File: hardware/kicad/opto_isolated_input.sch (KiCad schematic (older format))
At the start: 6 parts, among them Q1 BC547, Q2 BC337, U5 SFH617A-1

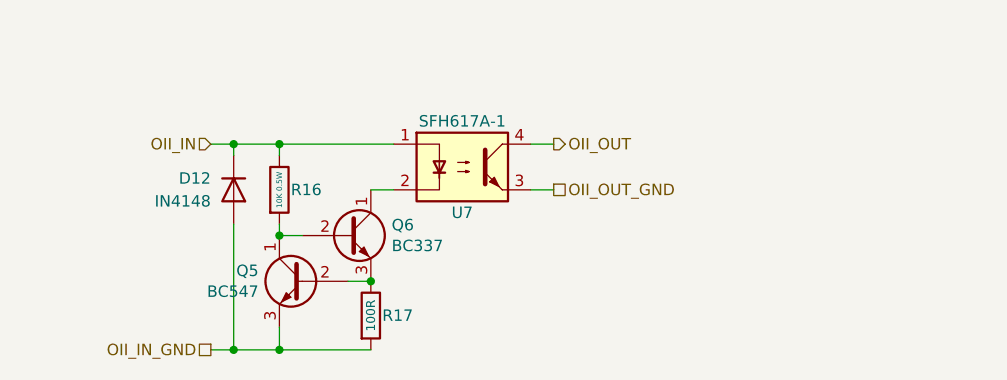
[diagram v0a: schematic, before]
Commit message: New board size
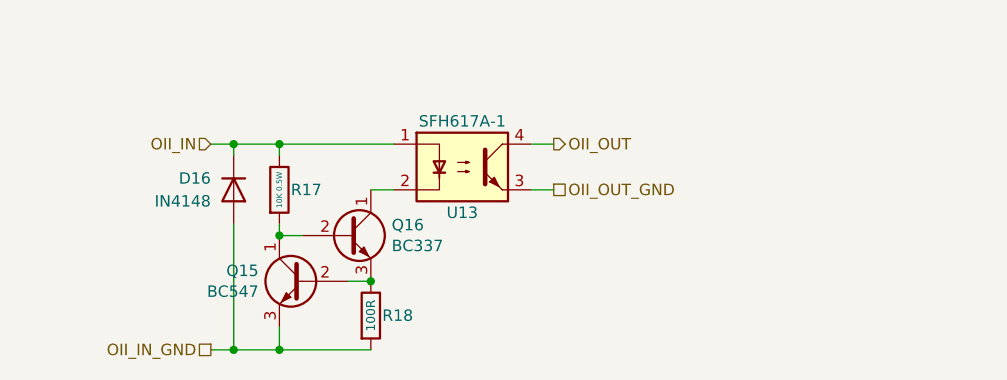
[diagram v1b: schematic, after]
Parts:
- renumbered D10 to D9, R12 to R3, R13 to R4, U5 to U6
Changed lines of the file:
@@
 $EndDescr
 $Comp
-L Isolator:SFH617A-1 U5
+L Isolator:SFH617A-1 U6
 U 1 1 62EBA913
 P 6100 3400
-AR Path="/62FB7846/62EBA913" Ref="U5"  Part="1"
-AR Path="/63089671/62EBA913" Ref="U6"  Part="1"
-AR Path="/63103CAF/62EBA913" Ref="U7"  Part="1"
-AR Path="/62F64647/62EBA913" Ref="U8"  Part="1"
-AR Path="/62FD589D/62EBA913" Ref="U9"  Part="1"
-AR Path="/63041ECA/62EBA913" Ref="U10"  Part="1"
-AR Path="/62F45EE0/62EBA913" Ref="U11"  Part="1"
-AR Path="/62FB890E/62EBA913" Ref="U12"  Part="1"
-F 0 "U7" H 6100 3200 50  0000 C CNN
+AR Path="/62FB7846/62EBA913" Ref="U6"  Part="1"
+AR Path="/63089671/62EBA913" Ref="U7"  Part="1"
+AR Path="/63103CAF/62EBA913" Ref="U8"  Part="1"
+AR Path="/62F64647/62EBA913" Ref="U9"  Part="1"
+AR Path="/62FD589D/62EBA913" Ref="U10"  Part="1"
+AR Path="/63041ECA/62EBA913" Ref="U11"  Part="1"
+AR Path="/62F45EE0/62EBA913" Ref="U12"  Part="1"
+AR Path="/62FB890E/62EBA913" Ref="U13"  Part="1"
+F 0 "U13" H 6100 3200 50  0000 C CNN
 F 1 "SFH617A-1" H 6100 3600 50  0000 C CNN
 F 2 "Package_DIP:DIP-4_W7.62mm" H 5900 3200 50  0001 L CIN
@@
 	5800 3500 5700 3500
 $Comp
-L Device:R R12
+L Device:R R3
 U 1 1 62ED7963
 P 5300 3500
-AR Path="/62FB7846/62ED7963" Ref="R12"  Part="1"
-AR Path="/63089671/62ED7963" Ref="R14"  Part="1"
-AR Path="/63103CAF/62ED7963" Ref="R16"  Part="1"
-AR Path="/62F64647/62ED7963" Ref="R18"  Part="1"
-AR Path="/62FD589D/62ED7963" Ref="R20"  Part="1"
-AR Path="/63041ECA/62ED7963" Ref="R22"  Part="1"
-AR Path="/62F45EE0/62ED7963" Ref="R24"  Part="1"
-AR Path="/62FB890E/62ED7963" Ref="R26"  Part="1"
-F 0 "R16" H 5350 3500 50  0000 L CNN
+AR Path="/62FB7846/62ED7963" Ref="R3"  Part="1"
+AR Path="/63089671/62ED7963" Ref="R5"  Part="1"
+AR Path="/63103CAF/62ED7963" Ref="R7"  Part="1"
+AR Path="/62F64647/62ED7963" Ref="R9"  Part="1"
+AR Path="/62FD589D/62ED7963" Ref="R11"  Part="1"
+AR Path="/63041ECA/62ED7963" Ref="R13"  Part="1"
+AR Path="/62F45EE0/62ED7963" Ref="R15"  Part="1"
+AR Path="/62FB890E/62ED7963" Ref="R17"  Part="1"
+F 0 "R17" H 5350 3500 50  0000 L CNN
 F 1 "10K 0.5W" V 5300 3500 24  0000 C CNN
 F 2 "Resistor_THT:R_Axial_DIN0207_L6.3mm_D2.5mm_P2.54mm_Vertical" V 5230 3500 50  0001 C CNN
@@
 Connection ~ 5300 3300
 $Comp
-L Device:R R13
+L Device:R R4
 U 1 1 62F493CD
 P 5700 4050
-AR Path="/62FB7846/62F493CD" Ref="R13"  Part="1"
-AR Path="/63089671/62F493CD" Ref="R15"  Part="1"
-AR Path="/63103CAF/62F493CD" Ref="R17"  Part="1"
-AR Path="/62F64647/62F493CD" Ref="R19"  Part="1"
-AR Path="/62FD589D/62F493CD" Ref="R21"  Part="1"
-AR Path="/63041ECA/62F493CD" Ref="R23"  Part="1"
-AR Path="/62F45EE0/62F493CD" Ref="R25"  Part="1"
-AR Path="/62FB890E/62F493CD" Ref="R27"  Part="1"
-F 0 "R17" H 5750 4050 50  0000 L CNN
+AR Path="/62FB7846/62F493CD" Ref="R4"  Part="1"
+AR Path="/63089671/62F493CD" Ref="R6"  Part="1"
+AR Path="/63103CAF/62F493CD" Ref="R8"  Part="1"
+AR Path="/62F64647/62F493CD" Ref="R10"  Part="1"
+AR Path="/62FD589D/62F493CD" Ref="R12"  Part="1"
+AR Path="/63041ECA/62F493CD" Ref="R14"  Part="1"
+AR Path="/62F45EE0/62F493CD" Ref="R16"  Part="1"
+AR Path="/62FB890E/62F493CD" Ref="R18"  Part="1"
+F 0 "R18" H 5750 4050 50  0000 L CNN
 F 1 "100R" V 5700 4050 39  0000 C CNN
 F 2 "Resistor_THT:R_Axial_DIN0207_L6.3mm_D2.5mm_P2.54mm_Vertical" V 5630 4050 50  0001 C CNN
@@
 AR Path="/62F45EE0/62EA87F7" Ref="Q14"  Part="1"
 AR Path="/62FB890E/62EA87F7" Ref="Q16"  Part="1"
-F 0 "Q6" H 5791 3746 50  0000 L CNN
+F 0 "Q16" H 5791 3746 50  0000 L CNN
 F 1 "BC337" H 5791 3655 50  0000 L CNN
 F 2 "Package_TO_SOT_THT:TO-92_Inline" H 5800 3625 50  0001 L CIN
@@
 Connection ~ 5300 4200
 $Comp
-L Simulation_SPICE:DIODE D10
+L Simulation_SPICE:DIODE D9
 U 1 1 62FE9B9E
 P 5100 3500
-AR Path="/62FB7846/62FE9B9E" Ref="D10"  Part="1"
-AR Path="/63089671/62FE9B9E" Ref="D11"  Part="1"
-AR Path="/63103CAF/62FE9B9E" Ref="D12"  Part="1"
-AR Path="/62F64647/62FE9B9E" Ref="D13"  Part="1"
-AR Path="/62FD589D/62FE9B9E" Ref="D14"  Part="1"
-AR Path="/63041ECA/62FE9B9E" Ref="D15"  Part="1"
-AR Path="/62F45EE0/62FE9B9E" Ref="D16"  Part="1"
-AR Path="/62FB890E/62FE9B9E" Ref="D17"  Part="1"
-F 0 "D12" V 5150 3600 50  0000 L CNN
+AR Path="/62FB7846/62FE9B9E" Ref="D9"  Part="1"
+AR Path="/63089671/62FE9B9E" Ref="D10"  Part="1"
+AR Path="/63103CAF/62FE9B9E" Ref="D11"  Part="1"
+AR Path="/62F64647/62FE9B9E" Ref="D12"  Part="1"
+AR Path="/62FD589D/62FE9B9E" Ref="D13"  Part="1"
+AR Path="/63041ECA/62FE9B9E" Ref="D14"  Part="1"
+AR Path="/62F45EE0/62FE9B9E" Ref="D15"  Part="1"
+AR Path="/62FB890E/62FE9B9E" Ref="D16"  Part="1"
+F 0 "D16" V 5150 3600 50  0000 L CNN
 F 1 "IN4148" V 5050 3600 50  0000 L CNN
 F 2 "Diode_THT:D_A-405_P2.54mm_Vertical_AnodeUp" H 5100 3500 50  0001 C CNN
@@
 AR Path="/62F45EE0/62FB7374" Ref="Q13"  Part="1"
 AR Path="/62FB890E/62FB7374" Ref="Q15"  Part="1"
-F 0 "Q5" H 5591 3946 50  0000 L CNN
+F 0 "Q15" H 5591 3946 50  0000 L CNN
 F 1 "BC547" H 5591 3855 50  0000 L CNN
 F 2 "Package_TO_SOT_THT:TO-92_Inline" H 5600 3825 50  0001 L CIN

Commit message: Stuff
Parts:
- added R19: 10K, Resistor_THT:R_Axial_DIN0207_L6.3mm_D2.5mm_P2.54mm_Vertical, symbol Device:R
- added U14: MAX6816, Package_TO_SOT_SMD:SOT-143, symbol Interface:MAX6816
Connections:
- net OII_IN_GND: now also R19.2, U14.1 (GND)
- net OII_OUT: now also U14.3 (OUT); no longer U6.4
- net OII_OUT_GND: no longer names the net of U6.3
- net OII_OUT_GND: now also R19.1, U14.2 (IN)
- new net OII_OUT_VCC: U14.4 (VCC), U6.4
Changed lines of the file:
@@
 $Descr A4 11693 8268
 encoding utf-8
-Sheet 4 9
+Sheet 2 9
 Title "SIM108 Switch Input Module"
 Date "2022-06-11"
@@
 AR Path="/62F45EE0/62EBA913" Ref="U12"  Part="1"
 AR Path="/62FB890E/62EBA913" Ref="U13"  Part="1"
-F 0 "U13" H 6100 3200 50  0000 C CNN
+F 0 "U6" H 6100 3200 50  0000 C CNN
 F 1 "SFH617A-1" H 6100 3600 50  0000 C CNN
 F 2 "Package_DIP:DIP-4_W7.62mm" H 5900 3200 50  0001 L CIN
@@
 AR Path="/62F45EE0/62ED7963" Ref="R15"  Part="1"
 AR Path="/62FB890E/62ED7963" Ref="R17"  Part="1"
-F 0 "R17" H 5350 3500 50  0000 L CNN
+F 0 "R3" H 5350 3500 50  0000 L CNN
 F 1 "10K 0.5W" V 5300 3500 24  0000 C CNN
 F 2 "Resistor_THT:R_Axial_DIN0207_L6.3mm_D2.5mm_P2.54mm_Vertical" V 5230 3500 50  0001 C CNN
@@
 AR Path="/62F45EE0/62F493CD" Ref="R16"  Part="1"
 AR Path="/62FB890E/62F493CD" Ref="R18"  Part="1"
-F 0 "R18" H 5750 4050 50  0000 L CNN
+F 0 "R4" H 5750 4050 50  0000 L CNN
 F 1 "100R" V 5700 4050 39  0000 C CNN
 F 2 "Resistor_THT:R_Axial_DIN0207_L6.3mm_D2.5mm_P2.54mm_Vertical" V 5630 4050 50  0001 C CNN
@@
 AR Path="/62F45EE0/62EA87F7" Ref="Q14"  Part="1"
 AR Path="/62FB890E/62EA87F7" Ref="Q16"  Part="1"
-F 0 "Q16" H 5791 3746 50  0000 L CNN
+F 0 "Q2" H 5791 3746 50  0000 L CNN
 F 1 "BC337" H 5791 3655 50  0000 L CNN
 F 2 "Package_TO_SOT_THT:TO-92_Inline" H 5800 3625 50  0001 L CIN
@@
 AR Path="/62F45EE0/62FE9B9E" Ref="D15"  Part="1"
 AR Path="/62FB890E/62FE9B9E" Ref="D16"  Part="1"
-F 0 "D16" V 5150 3600 50  0000 L CNN
+F 0 "D9" V 5150 3600 50  0000 L CNN
 F 1 "IN4148" V 5050 3600 50  0000 L CNN
 F 2 "Diode_THT:D_A-405_P2.54mm_Vertical_AnodeUp" H 5100 3500 50  0001 C CNN
@@
 Wire Wire Line
 	5100 4200 5300 4200
-Wire Wire Line
-	6400 3500 6500 3500
-Wire Wire Line
-	6400 3300 6500 3300
 $Comp
 L Transistor_BJT:BC547 Q1
@@
 AR Path="/62F45EE0/62FB7374" Ref="Q13"  Part="1"
 AR Path="/62FB890E/62FB7374" Ref="Q15"  Part="1"
-F 0 "Q15" H 5591 3946 50  0000 L CNN
+F 0 "Q1" H 5591 3946 50  0000 L CNN
 F 1 "BC547" H 5591 3855 50  0000 L CNN
 F 2 "Package_TO_SOT_THT:TO-92_Inline" H 5600 3825 50  0001 L CIN
@@
 Text HLabel 5000 4200 0    50   UnSpc ~ 0
 OII_IN_GND
-Text HLabel 6500 3300 2    50   Output ~ 0
+Text HLabel 7750 3750 2    50   Output ~ 0
 OII_OUT
-Text HLabel 6500 3500 2    50   UnSpc ~ 0
+Text HLabel 7750 4200 2    50   UnSpc ~ 0
 OII_OUT_GND
+$Comp
+L Interface:MAX6816 U14
+U 1 1 63451832
+P 7050 3750
+AR Path="/62FB7846/63451832" Ref="U14"  Part="1"
+AR Path="/63089671/63451832" Ref="U15"  Part="1"
+AR Path="/63103CAF/63451832" Ref="U16"  Part="1"
+AR Path="/62F64647/63451832" Ref="U17"  Part="1"
+AR Path="/62FD589D/63451832" Ref="U18"  Part="1"
+AR Path="/63041ECA/63451832" Ref="U19"  Part="1"
+AR Path="/62F45EE0/63451832" Ref="U20"  Part="1"
+AR Path="/62FB890E/63451832" Ref="U21"  Part="1"
+F 0 "U14" H 7150 4100 50  0000 L CNN
+F 1 "MAX6816" H 7100 3400 50  0000 L CNN
+F 2 "Package_TO_SOT_SMD:SOT-143" H 7700 3300 50  0001 C CNN
+F 3 "https://datasheets.maximintegrated.com/en/ds/1896.pdf" H 7050 3750 50  0001 C CNN
+	1    7050 3750
+	1    0    0    -1
+$EndComp
+Wire Wire Line
+	5700 4200 6600 4200
+Wire Wire Line
+	7050 4200 7050 4150
+Connection ~ 5700 4200
+Wire Wire Line
+	7050 4200 7750 4200
+Connection ~ 7050 4200
+Wire Wire Line
+	7050 3300 7050 3350
+Wire Wire Line
+	6400 3300 7050 3300
+Wire Wire Line
+	7050 3300 7750 3300
+Connection ~ 7050 3300
+Wire Wire Line
+	7350 3750 7750 3750
+Wire Wire Line
+	6600 3500 6600 3750
+Wire Wire Line
+	6600 3750 6750 3750
+Wire Wire Line
+	6400 3500 6600 3500
+Text HLabel 7750 3300 2    50   Input ~ 0
+OII_OUT_VCC
+$Comp
+L Device:R R19
+U 1 1 6345CD68
+P 6600 4050
+AR Path="/62FB7846/6345CD68" Ref="R19"  Part="1"
+AR Path="/63089671/6345CD68" Ref="R20"  Part="1"
+AR Path="/63103CAF/6345CD68" Ref="R21"  Part="1"
+AR Path="/62F64647/6345CD68" Ref="R22"  Part="1"
+AR Path="/62FD589D/6345CD68" Ref="R23"  Part="1"
+AR Path="/63041ECA/6345CD68" Ref="R24"  Part="1"
+AR Path="/62F45EE0/6345CD68" Ref="R25"  Part="1"
+AR Path="/62FB890E/6345CD68" Ref="R26"  Part="1"
+F 0 "R19" H 6650 4050 50  0000 L CNN
+F 1 "10K" V 6600 4050 39  0000 C CNN
+F 2 "Resistor_THT:R_Axial_DIN0207_L6.3mm_D2.5mm_P2.54mm_Vertical" V 6530 4050 50  0001 C CNN
+F 3 "~" H 6600 4050 50  0001 C CNN
+F 4 "0.125W" V 6700 4050 50  0001 C CNN "Power"
+	1    6600 4050
+	1    0    0    -1
+$EndComp
+Connection ~ 6600 4200
+Wire Wire Line
+	6600 4200 7050 4200
+Wire Wire Line
+	6600 3900 6600 3750
+Connection ~ 6600 3750
 $EndSCHEMATC

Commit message: Debounce
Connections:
- wire segments 26 -> 27
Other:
- moved on the sheet: U20
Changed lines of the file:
@@
 $Descr A4 11693 8268
 encoding utf-8
-Sheet 2 9
+Sheet 7 9
 Title "SIM108 Switch Input Module"
 Date "2022-06-11"
@@
 AR Path="/62F45EE0/62EBA913" Ref="U12"  Part="1"
 AR Path="/62FB890E/62EBA913" Ref="U13"  Part="1"
-F 0 "U6" H 6100 3200 50  0000 C CNN
+F 0 "U12" H 6100 3200 50  0000 C CNN
 F 1 "SFH617A-1" H 6100 3600 50  0000 C CNN
 F 2 "Package_DIP:DIP-4_W7.62mm" H 5900 3200 50  0001 L CIN
@@
 AR Path="/62F45EE0/62ED7963" Ref="R15"  Part="1"
 AR Path="/62FB890E/62ED7963" Ref="R17"  Part="1"
-F 0 "R3" H 5350 3500 50  0000 L CNN
+F 0 "R15" H 5350 3500 50  0000 L CNN
 F 1 "10K 0.5W" V 5300 3500 24  0000 C CNN
 F 2 "Resistor_THT:R_Axial_DIN0207_L6.3mm_D2.5mm_P2.54mm_Vertical" V 5230 3500 50  0001 C CNN
@@
 AR Path="/62F45EE0/62F493CD" Ref="R16"  Part="1"
 AR Path="/62FB890E/62F493CD" Ref="R18"  Part="1"
-F 0 "R4" H 5750 4050 50  0000 L CNN
+F 0 "R16" H 5750 4050 50  0000 L CNN
 F 1 "100R" V 5700 4050 39  0000 C CNN
 F 2 "Resistor_THT:R_Axial_DIN0207_L6.3mm_D2.5mm_P2.54mm_Vertical" V 5630 4050 50  0001 C CNN
@@
 AR Path="/62F45EE0/62EA87F7" Ref="Q14"  Part="1"
 AR Path="/62FB890E/62EA87F7" Ref="Q16"  Part="1"
-F 0 "Q2" H 5791 3746 50  0000 L CNN
+F 0 "Q14" H 5791 3746 50  0000 L CNN
 F 1 "BC337" H 5791 3655 50  0000 L CNN
 F 2 "Package_TO_SOT_THT:TO-92_Inline" H 5800 3625 50  0001 L CIN
@@
 AR Path="/62F45EE0/62FE9B9E" Ref="D15"  Part="1"
 AR Path="/62FB890E/62FE9B9E" Ref="D16"  Part="1"
-F 0 "D9" V 5150 3600 50  0000 L CNN
+F 0 "D15" V 5150 3600 50  0000 L CNN
 F 1 "IN4148" V 5050 3600 50  0000 L CNN
 F 2 "Diode_THT:D_A-405_P2.54mm_Vertical_AnodeUp" H 5100 3500 50  0001 C CNN
@@
 AR Path="/62F45EE0/62FB7374" Ref="Q13"  Part="1"
 AR Path="/62FB890E/62FB7374" Ref="Q15"  Part="1"
-F 0 "Q1" H 5591 3946 50  0000 L CNN
+F 0 "Q13" H 5591 3946 50  0000 L CNN
 F 1 "BC547" H 5591 3855 50  0000 L CNN
 F 2 "Package_TO_SOT_THT:TO-92_Inline" H 5600 3825 50  0001 L CIN
@@
 Text HLabel 5000 4200 0    50   UnSpc ~ 0
 OII_IN_GND
-Text HLabel 7750 3750 2    50   Output ~ 0
+Text HLabel 7600 3300 2    50   Output ~ 0
 OII_OUT
-Text HLabel 7750 4200 2    50   UnSpc ~ 0
+Text HLabel 7600 4200 2    50   UnSpc ~ 0
 OII_OUT_GND
 $Comp
 L Interface:MAX6816 U14
 U 1 1 63451832
-P 7050 3750
+P 6900 3300
 AR Path="/62FB7846/63451832" Ref="U14"  Part="1"
 AR Path="/63089671/63451832" Ref="U15"  Part="1"
@@
 AR Path="/62F45EE0/63451832" Ref="U20"  Part="1"
 AR Path="/62FB890E/63451832" Ref="U21"  Part="1"
-F 0 "U14" H 7150 4100 50  0000 L CNN
-F 1 "MAX6816" H 7100 3400 50  0000 L CNN
-F 2 "Package_TO_SOT_SMD:SOT-143" H 7700 3300 50  0001 C CNN
-F 3 "https://datasheets.maximintegrated.com/en/ds/1896.pdf" H 7050 3750 50  0001 C CNN
-	1    7050 3750
-	1    0    0    -1
-$EndComp
-Wire Wire Line
-	5700 4200 6600 4200
-Wire Wire Line
-	7050 4200 7050 4150
-Connection ~ 5700 4200
-Wire Wire Line
-	7050 4200 7750 4200
-Connection ~ 7050 4200
-Wire Wire Line
-	7050 3300 7050 3350
-Wire Wire Line
-	6400 3300 7050 3300
-Wire Wire Line
-	7050 3300 7750 3300
-Connection ~ 7050 3300
-Wire Wire Line
-	7350 3750 7750 3750
-Wire Wire Line
-	6600 3500 6600 3750
-Wire Wire Line
-	6600 3750 6750 3750
-Wire Wire Line
-	6400 3500 6600 3500
-Text HLabel 7750 3300 2    50   Input ~ 0
+F 0 "U20" H 7000 3650 50  0000 L CNN
+F 1 "MAX6816" H 6950 2950 50  0000 L CNN
+F 2 "Package_TO_SOT_SMD:SOT-143" H 7550 2850 50  0001 C CNN
+F 3 "https://datasheets.maximintegrated.com/en/ds/1896.pdf" H 6900 3300 50  0001 C CNN
+	1    6900 3300
+	1    0    0    -1
+$EndComp
+Wire Wire Line
+	6400 3300 6500 3300
+Wire Wire Line
+	7200 3300 7600 3300
+Text HLabel 7600 2800 2    50   Input ~ 0
 OII_OUT_VCC
 $Comp
 L Device:R R19
-U 1 1 6345CD68
-P 6600 4050
-AR Path="/62FB7846/6345CD68" Ref="R19"  Part="1"
-AR Path="/63089671/6345CD68" Ref="R20"  Part="1"
-AR Path="/63103CAF/6345CD68" Ref="R21"  Part="1"
-AR Path="/62F64647/6345CD68" Ref="R22"  Part="1"
-AR Path="/62FD589D/6345CD68" Ref="R23"  Part="1"
-AR Path="/63041ECA/6345CD68" Ref="R24"  Part="1"
-AR Path="/62F45EE0/6345CD68" Ref="R25"  Part="1"
-AR Path="/62FB890E/6345CD68" Ref="R26"  Part="1"
-F 0 "R19" H 6650 4050 50  0000 L CNN
-F 1 "10K" V 6600 4050 39  0000 C CNN
-F 2 "Resistor_THT:R_Axial_DIN0207_L6.3mm_D2.5mm_P2.54mm_Vertical" V 6530 4050 50  0001 C CNN
-F 3 "~" H 6600 4050 50  0001 C CNN
-F 4 "0.125W" V 6700 4050 50  0001 C CNN "Power"
-	1    6600 4050
-	1    0    0    -1
-$EndComp
-Connection ~ 6600 4200
-Wire Wire Line
-	6600 4200 7050 4200
-Wire Wire Line
-	6600 3900 6600 3750
-Connection ~ 6600 3750
+U 1 1 6343512B
+P 6500 3100
+AR Path="/62FB7846/6343512B" Ref="R19"  Part="1"
+AR Path="/63089671/6343512B" Ref="R20"  Part="1"
+AR Path="/63103CAF/6343512B" Ref="R21"  Part="1"
+AR Path="/62F64647/6343512B" Ref="R22"  Part="1"
+AR Path="/62FD589D/6343512B" Ref="R23"  Part="1"
+AR Path="/63041ECA/6343512B" Ref="R24"  Part="1"
+AR Path="/62F45EE0/6343512B" Ref="R25"  Part="1"
+AR Path="/62FB890E/6343512B" Ref="R26"  Part="1"
+F 0 "R25" H 6550 3100 50  0000 L CNN
+F 1 "10K" V 6500 3100 39  0000 C CNN
+F 2 "Resistor_THT:R_Axial_DIN0207_L6.3mm_D2.5mm_P2.54mm_Vertical" V 6430 3100 50  0001 C CNN
+F 3 "~" H 6500 3100 50  0001 C CNN
+F 4 "0.125W" V 6600 3100 50  0001 C CNN "Power"
+	1    6500 3100
+	1    0    0    -1
+$EndComp
+Wire Wire Line
+	6500 3250 6500 3300
+Wire Wire Line
+	6500 3300 6600 3300
+Connection ~ 6500 3300
+Wire Wire Line
+	6400 3500 6500 3500
+Wire Wire Line
+	6500 3500 6500 4200
+Wire Wire Line
+	6900 3700 6900 4200
+Wire Wire Line
+	6900 4200 7650 4200
+Wire Wire Line
+	6500 2800 6900 2800
+Wire Wire Line
+	6500 2800 6500 2950
+Wire Wire Line
+	6900 2900 6900 2800
+Connection ~ 6900 2800
+Wire Wire Line
+	6900 2800 7600 2800
+Wire Wire Line
+	6500 4200 6900 4200
+Connection ~ 6900 4200
 $EndSCHEMATC
